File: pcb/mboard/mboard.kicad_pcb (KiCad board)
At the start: 2 copper layers, 108.5 x 74.9 mm, 13 parts, among them J1 AudioJack3_SwitchTR, U1 SD Card holder

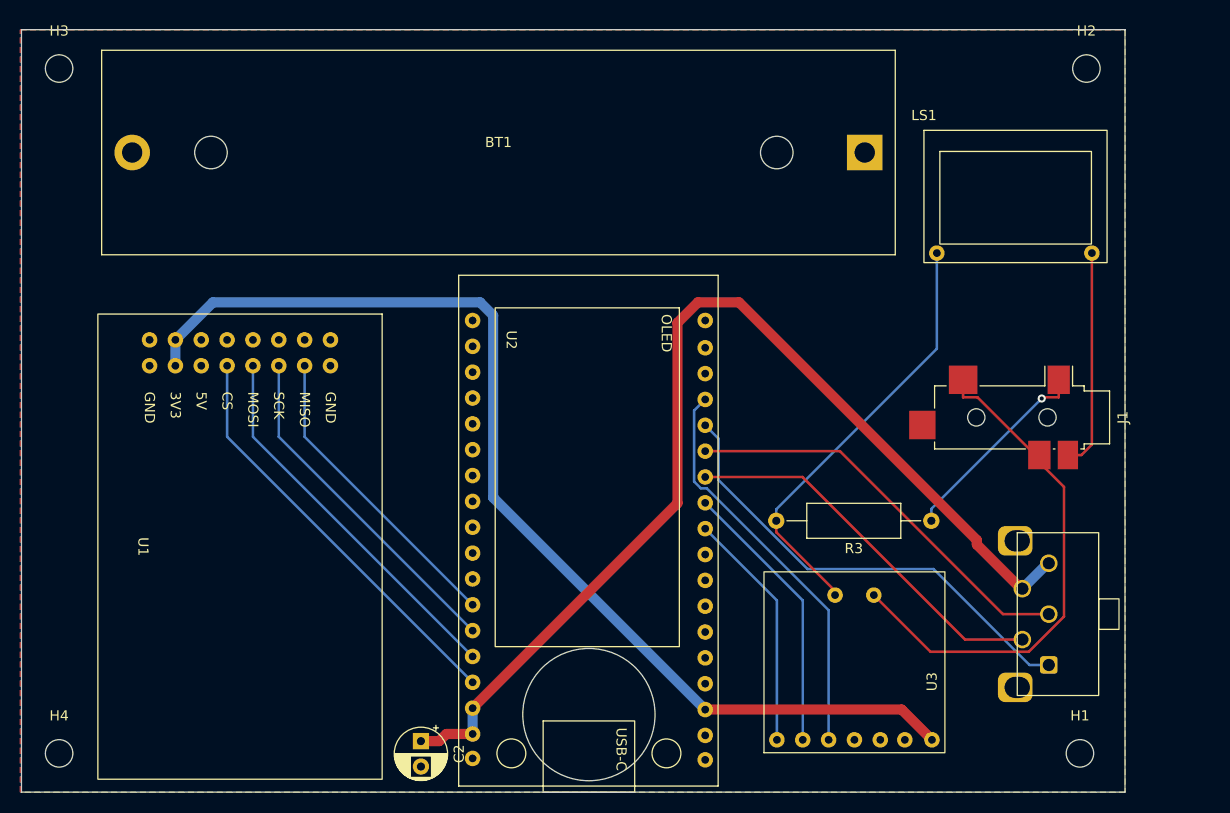
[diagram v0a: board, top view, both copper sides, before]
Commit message: added global settings menu added new settings: screen rotation, rotary encoder speed and direction more documentation
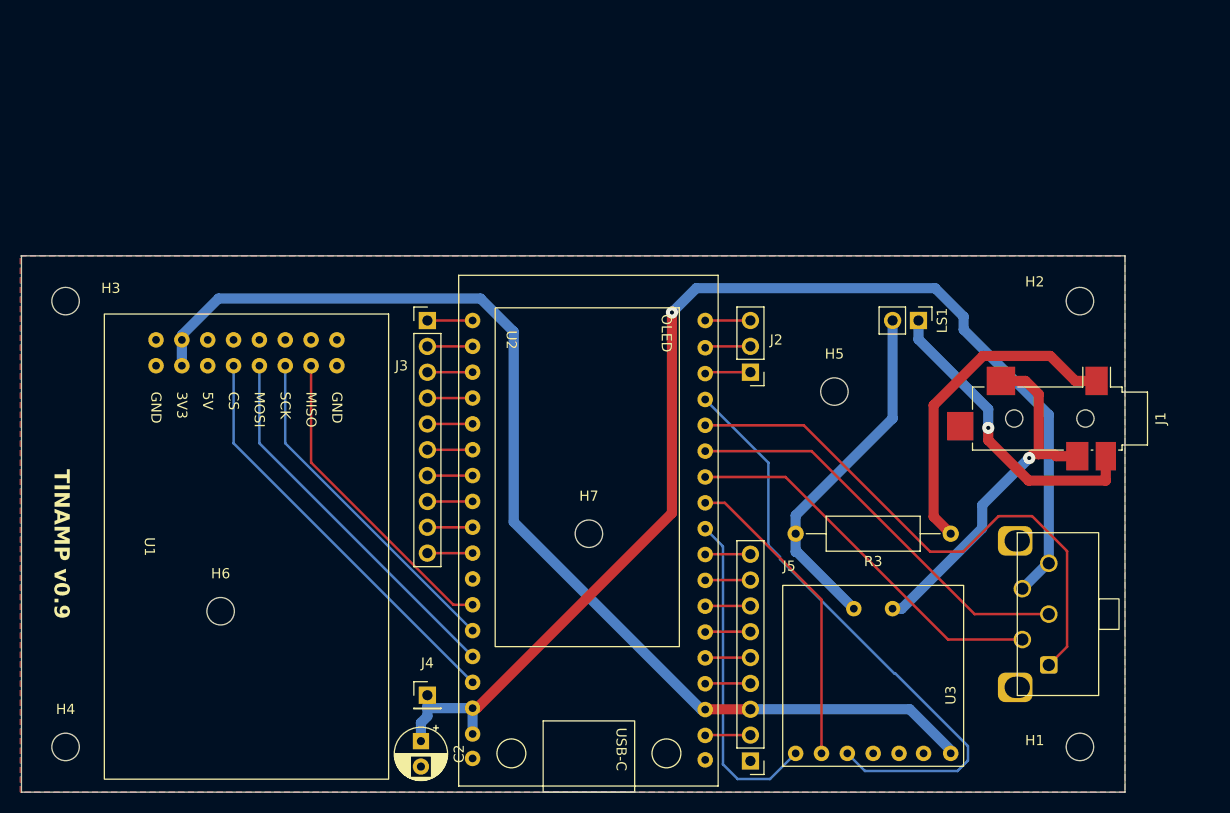
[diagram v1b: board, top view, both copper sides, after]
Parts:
- removed BT1: Battery_Cell, Battery:BatteryHolder_MPD_BH-18650-PC2
- added H5: MountingHole, MountingHole:MountingHole_2.7mm, F.Cu at (125.1, 87.6)
- added H6: MountingHole, MountingHole:MountingHole_2.7mm, F.Cu at (64.8, 109.2)
- added H7: MountingHole, MountingHole:MountingHole_2.7mm, F.Cu at (101.0, 101.6)
- added J2: Conn_01x03_Pin, Connector_PinHeader_2.54mm:PinHeader_1x03_P2.54mm_Vertical, F.Cu at (116.8, 85.7)
- added J3: Conn_01x10_Pin, Connector_PinHeader_2.54mm:PinHeader_1x10_P2.54mm_Vertical, F.Cu at (85.1, 80.7)
- added J4: Conn_01x01_Pin, Connector_PinHeader_2.54mm:PinHeader_1x01_P2.54mm_Vertical, F.Cu at (85.1, 117.5)
- added J5: Conn_01x09_Pin, Connector_PinHeader_2.54mm:PinHeader_1x09_P2.54mm_Vertical, F.Cu at (116.8, 123.9)
- LS1: footprint components:OWS-131845W50A-8 -> Connector_PinHeader_2.54mm:PinHeader_1x02_P2.54mm_Vertical
- moved H2 22.9 mm to (149.2, 78.7)
- moved H3 22.9 mm to (49.5, 78.7)
- moved LS1 19.7 mm to (133.4, 80.6), turned to -90 degrees
- moved J1 3.73 mm to (147.3, 90.3)
- moved R3 2.29 mm to (136.5, 101.6)
- moved U3 2.27 mm to (120.0, 124.5)
- moved H4 0.90 mm to (49.5, 122.6)
- moved U1 0.64 mm to (53.3, 102.9)
- moved H1 0.63 mm to (149.2, 122.6)
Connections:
- J1 pad RN: Net-(J1-PadRN) -> Net-(LS1-Pin_1)
- LS1 pad 1: Net-(U3-SP-) -> Net-(LS1-Pin_1)
- LS1 pad 2: Net-(J1-PadRN) -> Net-(LS1-Pin_2)
- R3 pad 2: Net-(U3-SP-) -> Net-(LS1-Pin_2)
- U2 pad J2_16: unconnected-(U2-3-PadJ2_16) -> Net-(J2-Pin_1)
- U2 pad J2_17: unconnected-(U2-2-PadJ2_17) -> Net-(J2-Pin_2)
- U2 pad J2_18: unconnected-(U2-1-PadJ2_18) -> Net-(J2-Pin_3)
- U2 pad J2_2: unconnected-(U2-5V-PadJ2_2) -> Net-(J5-Pin_2)
- U2 pad J2_4: unconnected-(U2-Ve-PadJ2_4) -> Net-(J5-Pin_4)
- U2 pad J2_5: unconnected-(U2-44-PadJ2_5) -> Net-(J5-Pin_5)
- U2 pad J2_6: unconnected-(U2-43-PadJ2_6) -> Net-(J5-Pin_6)
- U2 pad J2_7: unconnected-(U2-RST-PadJ2_7) -> Net-(J5-Pin_7)
- U2 pad J2_8: unconnected-(U2-0-PadJ2_8) -> Net-(J5-Pin_8)
- U2 pad J2_9: unconnected-(U2-21-PadJ2_9) -> Net-(J5-Pin_9)
- U2 pad J3_10: unconnected-(U2-36-PadJ3_10) -> Net-(J3-Pin_9)
- U2 pad J3_11: unconnected-(U2-37-PadJ3_11) -> Net-(J3-Pin_8)
- U2 pad J3_12: unconnected-(U2-38-PadJ3_12) -> Net-(J3-Pin_7)
- U2 pad J3_13: unconnected-(U2-39-PadJ3_13) -> Net-(J3-Pin_6)
- U2 pad J3_14: unconnected-(U2-40-PadJ3_14) -> Net-(J3-Pin_5)
- U2 pad J3_15: unconnected-(U2-41-PadJ3_15) -> Net-(J3-Pin_4)
- U2 pad J3_16: unconnected-(U2-42-PadJ3_16) -> Net-(J3-Pin_3)
- U2 pad J3_17: unconnected-(U2-45-PadJ3_17) -> Net-(J3-Pin_2)
- U2 pad J3_18: unconnected-(U2-46-PadJ3_18) -> Net-(J3-Pin_1)
- U2 pad J3_9: unconnected-(U2-35-PadJ3_9) -> Net-(J3-Pin_10)
- U3 pad 8: Net-(U3-SP-) -> Net-(LS1-Pin_2)
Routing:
- net Net-(U3-SP-): track 42.5 -> 0.00 mm
- net Net-(LS1-Pin_2): track 0.00 -> 34.7 mm
- net Net-(LS1-Pin_1): track 0.00 -> 30.2 mm, vias 0 -> 1
- net Net-(J1-PadRN): track 21.6 -> 0.00 mm
- net Net-(U2-4): track 39.7 -> 59.2 mm
- net VCC: track 104.4 -> 121.2 mm, vias 0 -> 1
- net Net-(U3-SP+): track 51.4 -> 36.0 mm, vias 0 -> 1
- net Net-(J1-PadS): track 20.0 -> 32.4 mm, vias 1 -> 0
- net Net-(U2-5): track 45.9 -> 55.5 mm
- net Net-(U2-20): track 23.7 -> 32.7 mm
- net Net-(J2-Pin_2): track 0.00 -> 4.50 mm
- net Net-(J2-Pin_1): track 0.00 -> 4.50 mm
- net Net-(J5-Pin_8): track 0.00 -> 4.46 mm
- net Net-(J5-Pin_6): track 0.00 -> 4.46 mm
- net Net-(J5-Pin_5): track 0.00 -> 4.46 mm
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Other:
- board size 108.5 x 74.9 mm -> 108.5 x 52.7 mm
- board text added: "TINAMP v0.9"
